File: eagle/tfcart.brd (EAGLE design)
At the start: 71.9 x 55.5 mm, 19 parts, among them CN1 MSX_CART, IC7 AT27C020-55JUPLCCS32, IC8 LM1117MPX-3.3

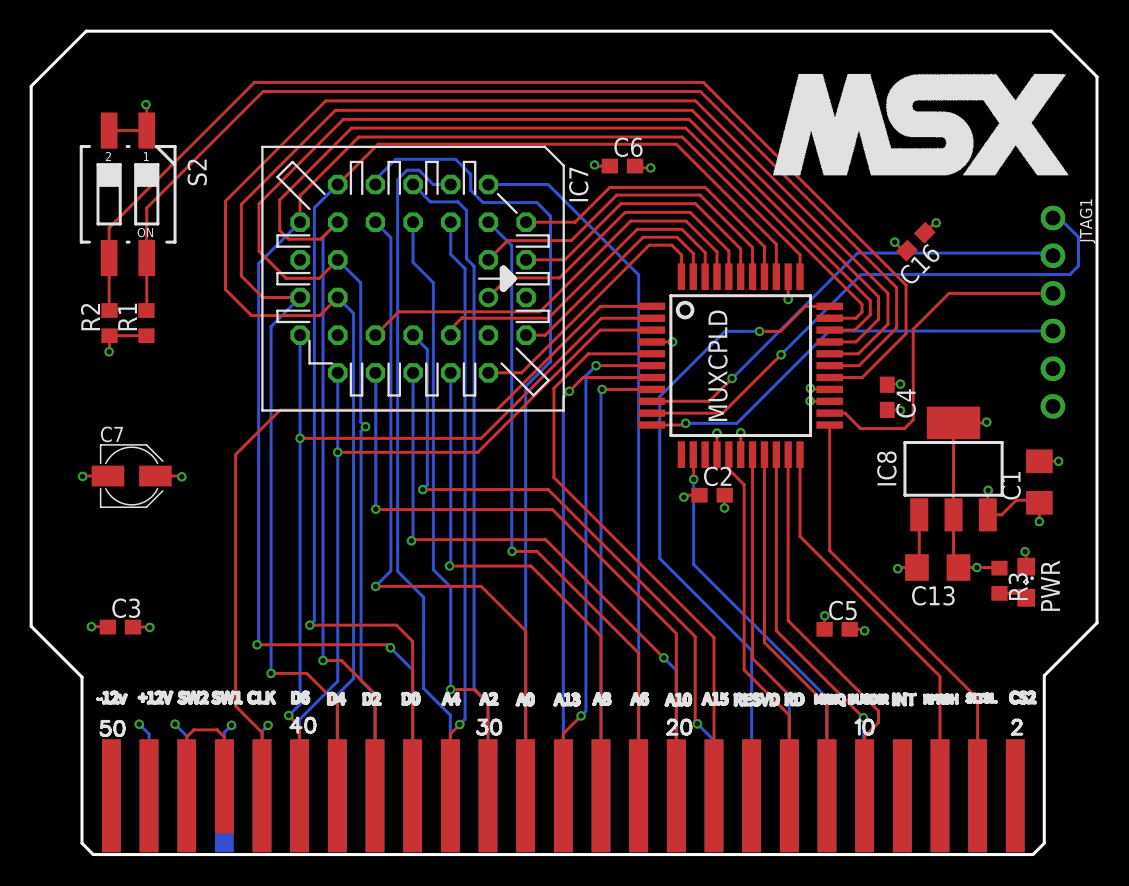
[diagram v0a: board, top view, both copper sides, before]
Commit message: fixed the drills fixed the corners changed the dip switches for jumpers.
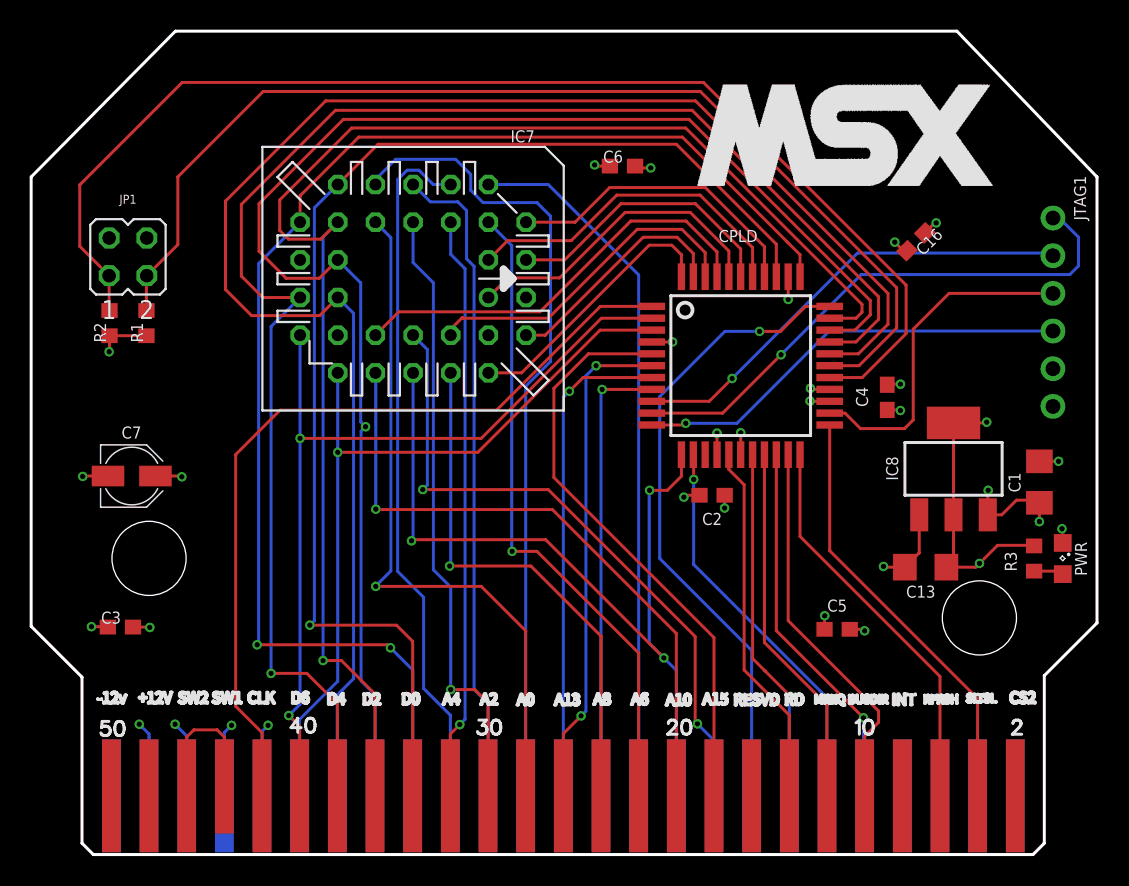
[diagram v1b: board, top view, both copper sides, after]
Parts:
- removed S2: 219-02, switch-dil:CTS-219-02
- added JP1: (no value), jumper:JP2Q
- CPLD: value XC9536_44VQ -> XC9536XL-10VQ44C
- moved PWR 2.94 mm to (66.2, 21.5)
- moved R3 2.78 mm to (64.3, 21.5)
- moved C13 0.81 mm to (56.9, 20.9)
- renumbered MUXCPLD to CPLD
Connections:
- net A11: now also CPLD.12
- net GND: now also JP1.2, JP1.4; no longer S2.1, S2.2
- net SW0: now also JP1.3; no longer S2.4
- net SW1: now also JP1.1; no longer S2.3
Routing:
- net A11: track 41.4 -> 57.1 mm, vias 2 -> 3
- net SW1: track 78.7 -> 83.2 mm
- net GND: track 33.5 -> 29.6 mm, vias 16 -> 15
- net VCC33: track 23.2 -> 27.0 mm
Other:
- outline, holes or cut-outs redrawn

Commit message: fixing the docker build and commiting everyting
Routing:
- net D3: track 100.0 -> 99.7 mm, vias 1 -> 0
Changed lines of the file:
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@@
 <contactref element="CN1" pad="P35"/>
 <wire x1="17.2974" y1="41.656" x2="18.8468" y2="40.1066" width="0.2032" layer="16"/>
-<wire x1="18.8722" y1="30.1018" x2="18.8722" y2="13.2588" width="0.2032" layer="16"/>
-<wire x1="18.8722" y1="13.2588" x2="19.812" y2="12.319" width="0.2032" layer="16"/>
+<wire x1="18.8468" y1="13.2842" x2="19.1643" y2="12.9667" width="0.2032" layer="16"/>
+<wire x1="19.1643" y1="12.9667" x2="19.812" y2="12.319" width="0.2032" layer="16"/>
 <wire x1="19.812" y1="12.319" x2="19.812" y2="5.5118" width="0.2032" layer="16"/>
-<wire x1="18.8722" y1="30.1018" x2="19.1742" y2="30.4038" width="0.2032" layer="16"/>
-<via x="19.1742" y="30.4038" extent="1-16" drill="0.35"/>
-<wire x1="19.1742" y1="30.4038" x2="18.8468" y2="30.7312" width="0.2032" layer="16"/>
-<wire x1="18.8468" y1="30.7312" x2="18.8468" y2="40.1066" width="0.2032" layer="16"/>
 <wire x1="17.2974" y1="41.656" x2="16.0528" y2="40.4114" width="0.2032" layer="1"/>
 <wire x1="13.8176" y1="40.4114" x2="11.9888" y2="42.2402" width="0.2032" layer="1"/>
@@
 <wire x1="40.9956" y1="51.1302" x2="53.213" y2="38.9128" width="0.2032" layer="1"/>
 <wire x1="52.184" y1="36.9186" x2="50.4754" y2="36.9186" width="0.2032" layer="1"/>
+<wire x1="18.8468" y1="40.1066" x2="18.8468" y2="13.2842" width="0.2032" layer="16"/>
 </signal>
 <signal name="D2">
